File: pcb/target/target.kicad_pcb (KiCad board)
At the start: 2 copper layers, 46 x 85.8 mm, 26 parts, among them J1 Pogo_01x06_female, J2 Pogo_01x06_male, J3 Conn_01x03_Pin, J4 Conn_01x03_Pin, J5 Piezo, Q1 SI2333CDS-HXY

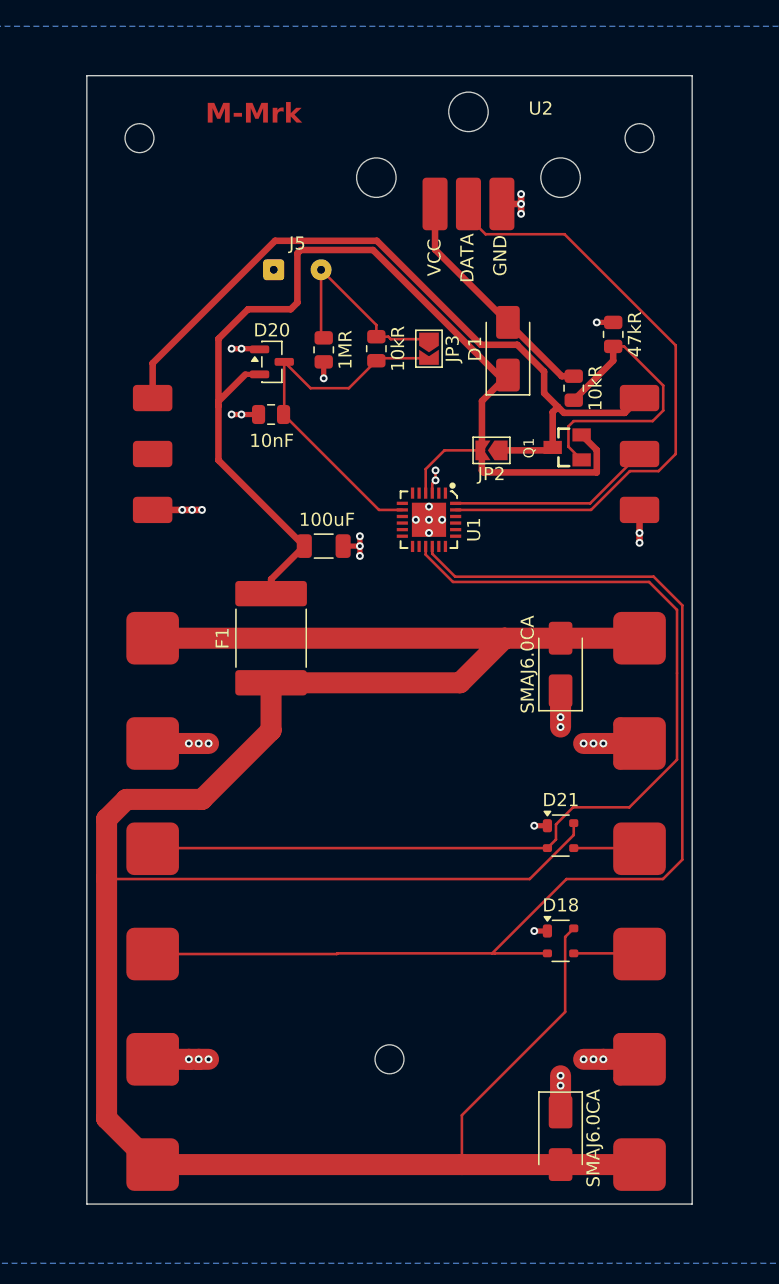
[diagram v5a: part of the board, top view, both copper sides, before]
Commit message: Switched to attiny1614 and fixed esd for the i2c lines (target pcb)
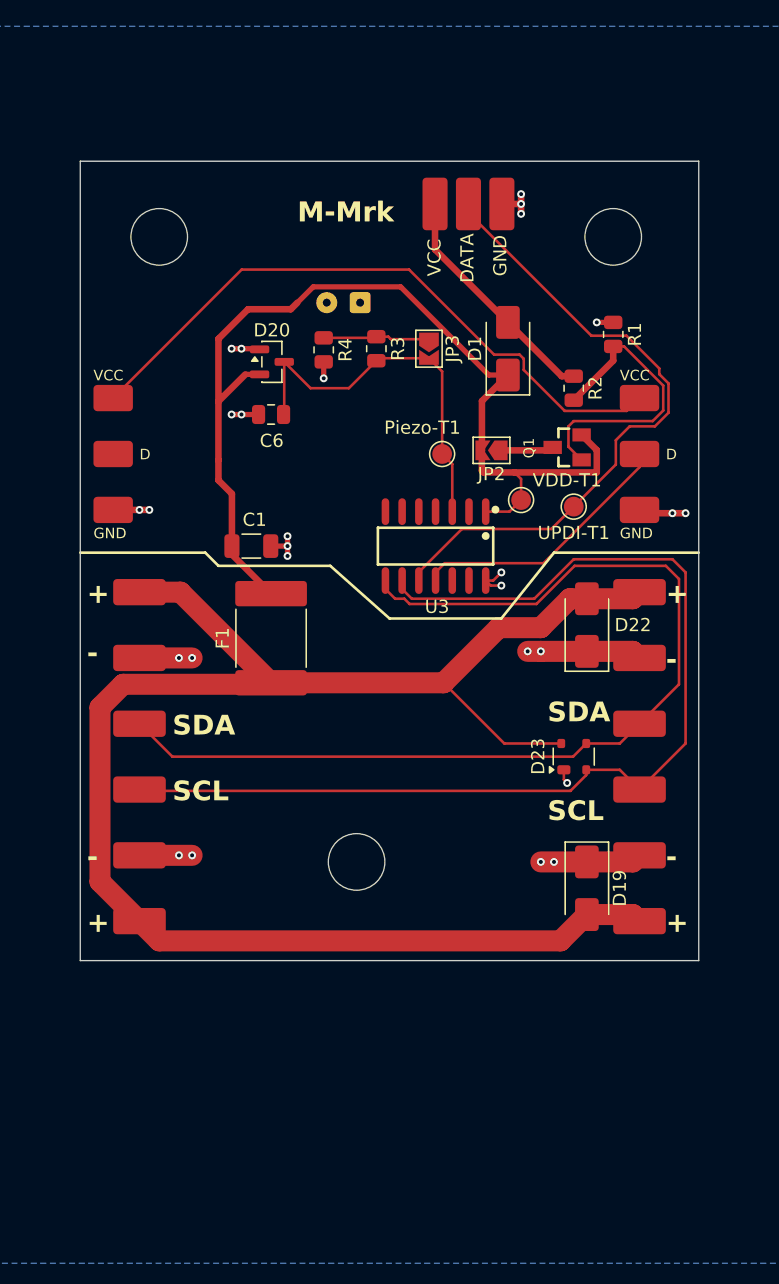
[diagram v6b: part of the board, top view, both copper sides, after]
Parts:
- removed D18, D21: PRTR5V0U2X, Package_TO_SOT_SMD:SOT-143
- removed the REF** at (77.0, 43.0)
- removed the REF** at (39.0, 43.0)
- removed the REF** at (58.0, 113.0)
- removed U1: ~, custom_footprints:WQFN-24_L4.0-W4.0-P0.50-TL-EP2.6
- added D23: PRTR5V0U2X, Package_TO_SOT_SMD:SOT-143, F.Cu at (72.0, 90.0)
- added Piezo-T1: TestPoint, TestPoint:TestPoint_Pad_D1.5mm, F.Cu at (62.0, 67.0)
- added REF**: MountingHole_4.3mm_M4, MountingHole:MountingHole_4.3mm_M4, F.Cu at (75.0, 50.5)
- added REF**: MountingHole_4.3mm_M4, MountingHole:MountingHole_4.3mm_M4, F.Cu at (55.5, 98.0)
- added REF**: MountingHole_4.3mm_M4, MountingHole:MountingHole_4.3mm_M4, F.Cu at (40.5, 50.5)
- added U3: ~, custom_footprints:SOIC-14_L8.7-W3.9-P1.27-LS6.0-BL, F.Cu at (61.5, 74.0)
- added UPDI-T1: TestPoint, TestPoint:TestPoint_Pad_D1.5mm, F.Cu at (72.0, 71.0)
- added VDD-T1: TestPoint, TestPoint:TestPoint_Pad_D1.5mm, F.Cu at (68.0, 70.5)
- moved D19 19.1 mm to (73.0, 100.0)
- moved J1 11.0 mm to (39.0, 90.0)
- moved J2 11.0 mm to (77.0, 90.0)
- moved J5 7.03 mm to (55.8, 55.5), turned to 180 degrees
- moved C1 5.50 mm to (47.5, 74.0)
- moved D22 3.61 mm to (73.0, 80.0)
- moved J4 3.00 mm to (37.0, 67.0)
- renumbered 100uF to C1, 10nF to C6, SMAJ6.0CA to D19, SMAJ6.0CA to D22, 47kR to R1, 10kR to R2, 10kR to R3, 1MR to R4
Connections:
- J2 pad 3: /ESD/SDA OUT -> SDA
- J2 pad 4: /ESD/SCL OUT -> SCL
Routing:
- net +5V Main: track 199.0 -> 125.5 mm
- net GND Main: track 64.1 -> 47.1 mm, vias 42 -> 27
- net Net-(J5-OUT): track 16.2 -> 8.11 mm
- net +5V: track 84.9 -> 77.4 mm
- net SCL: track 87.9 -> 81.7 mm
- net /ESD/SDA OUT: track 5.02 -> 0.00 mm
- net /ESD/SCL OUT: track 5.02 -> 0.00 mm
- net LED data: track 15.5 -> 20.4 mm
- net /LED Circle/VCC: track 57.6 -> 53.4 mm
- net UPDI pin: track 47.5 -> 49.4 mm
- net SDA: track 76.2 -> 77.4 mm
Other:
- board size 46 x 85.8 mm -> 47 x 60.8 mm
- board text added: "+"
- board text added: "-"
- board text added: "D"
- board text added: "GND"
- board text added: "SCL"
- board text added: "SDA"
- board text added: "VCC"

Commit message: exported and adjusted target pcb
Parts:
- moved REF** 2.50 mm to (58.0, 98.0)
- moved REF** 0.50 mm to (75.5, 50.5)
- moved R1 0.09 mm to (75.0, 58.0)
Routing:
- net /LED Circle/VCC: track 53.4 -> 58.2 mm
- net Net-(J5-OUT): track 8.11 -> 10.9 mm
- net +5V: track 77.4 -> 76.4 mm
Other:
- board text added: "Blitzpong Target PCB"
- board text added: "V2"
